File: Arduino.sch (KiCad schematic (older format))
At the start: 0 parts

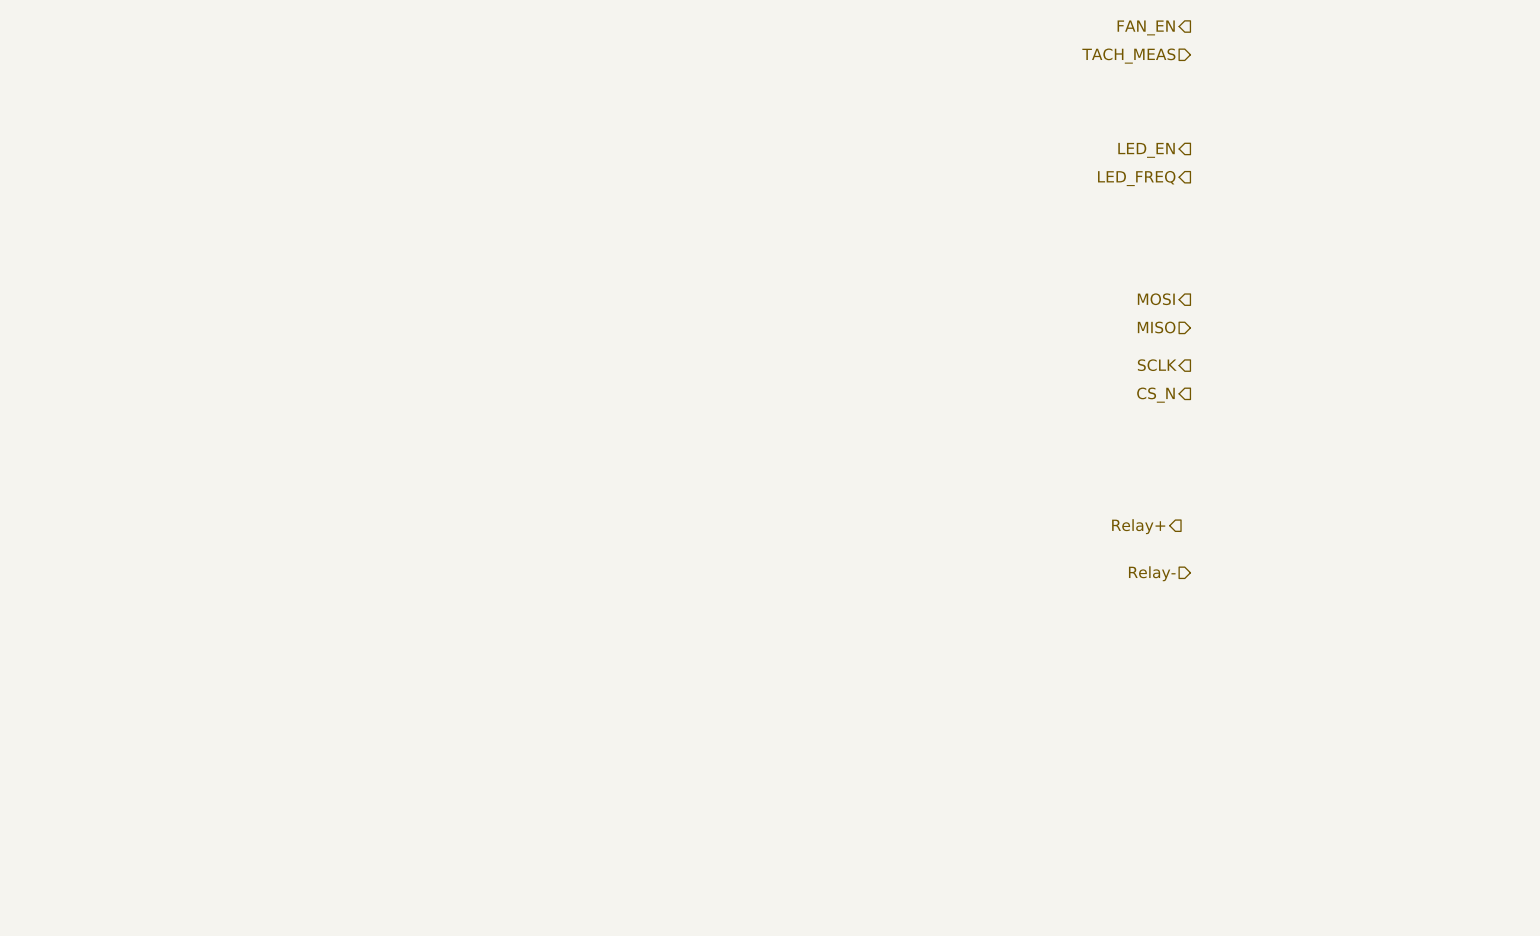
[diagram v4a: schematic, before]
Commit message: Create Arduino Schematic and Wire Up top Level
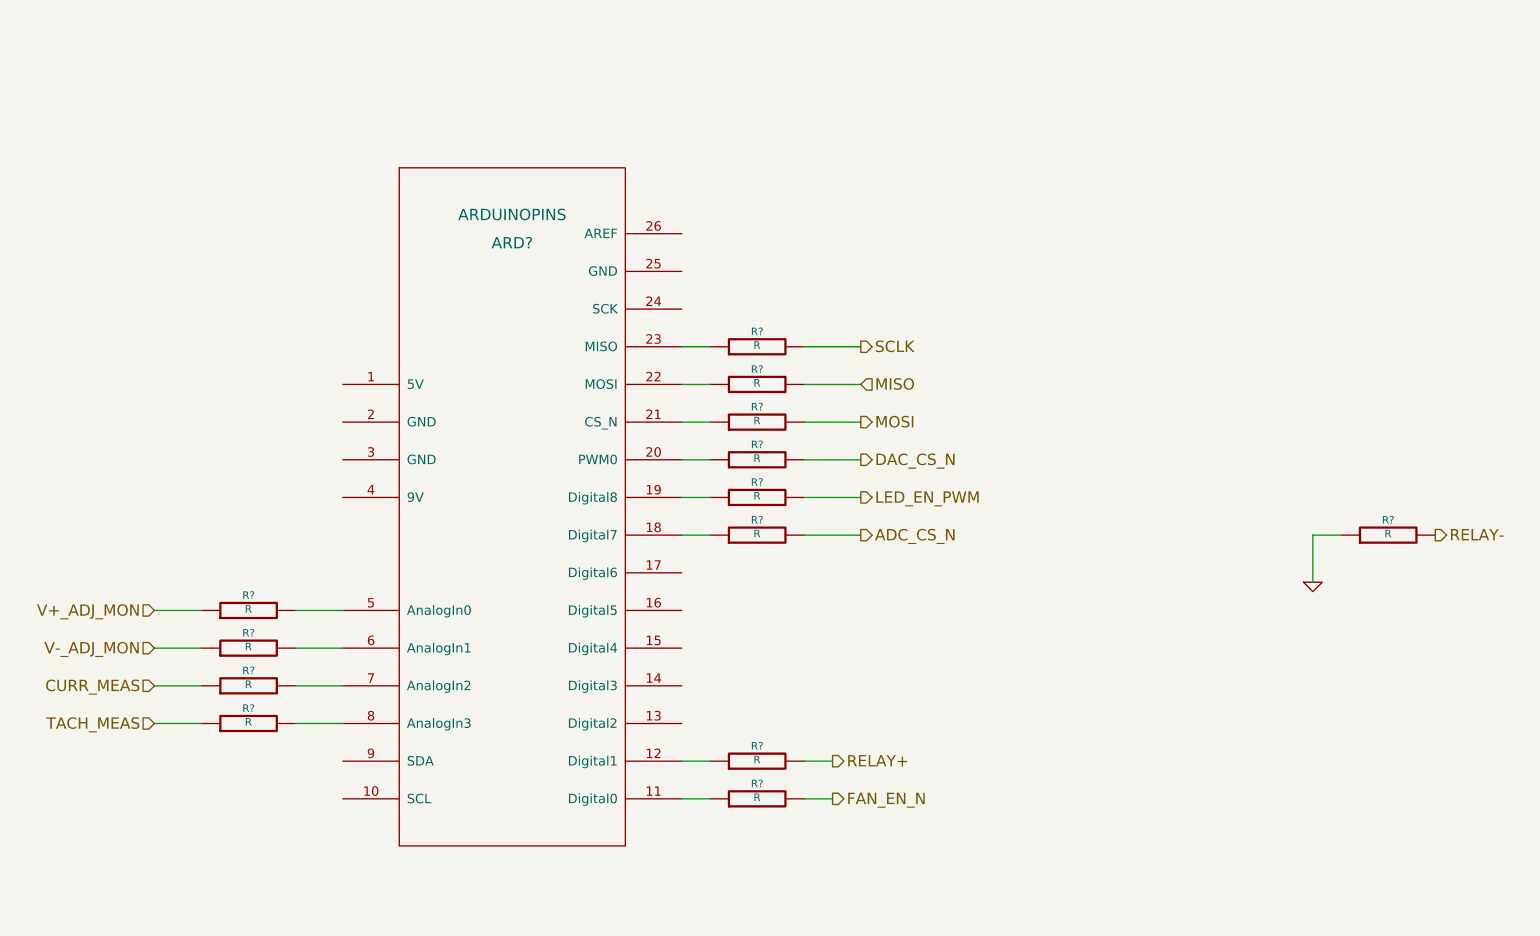
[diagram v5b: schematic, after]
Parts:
- added ARD?: ARDUINOPINS, symbol ARDUINOPINS
- added R? (x13): R, ~, symbol R
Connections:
- net MISO: now also R?.2
- net MOSI: now also R?.2
- net SCLK: now also R?.2
- net TACH_MEAS: now also R?.1
- new net: ARD?.11 (Digital0), R?.1
- new net: ARD?.12 (Digital1), R?.1
- new net: ARD?.18 (Digital7), R?.1
- new net: ARD?.19 (Digital8), R?.1
- new net: ARD?.20 (PWM0), R?.1
- new net: ARD?.21 (CS_N), R?.1
- new net: ARD?.22 (MOSI), R?.1
- new net: ARD?.23 (MISO), R?.1
- new net: ARD?.5 (AnalogIn0), R?.2
- new net: ARD?.6 (AnalogIn1), R?.2
- new net: ARD?.7 (AnalogIn2), R?.2
- new net: ARD?.8 (AnalogIn3), R?.2
- new net ADC_CS_N: R?.2
- new net CURR_MEAS: R?.1
- new net DAC_CS_N: R?.2
- new net FAN_EN_N: R?.2
- new net GND: R?.1
- new net LED_EN_PWM: R?.2
- new net RELAY+: R?.2
- new net RELAY-: R?.2
- new net V+_ADJ_MON: R?.1
- new net V-_ADJ_MON: R?.1

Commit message: Upgrade Current/Fan Output Schem Use PWM
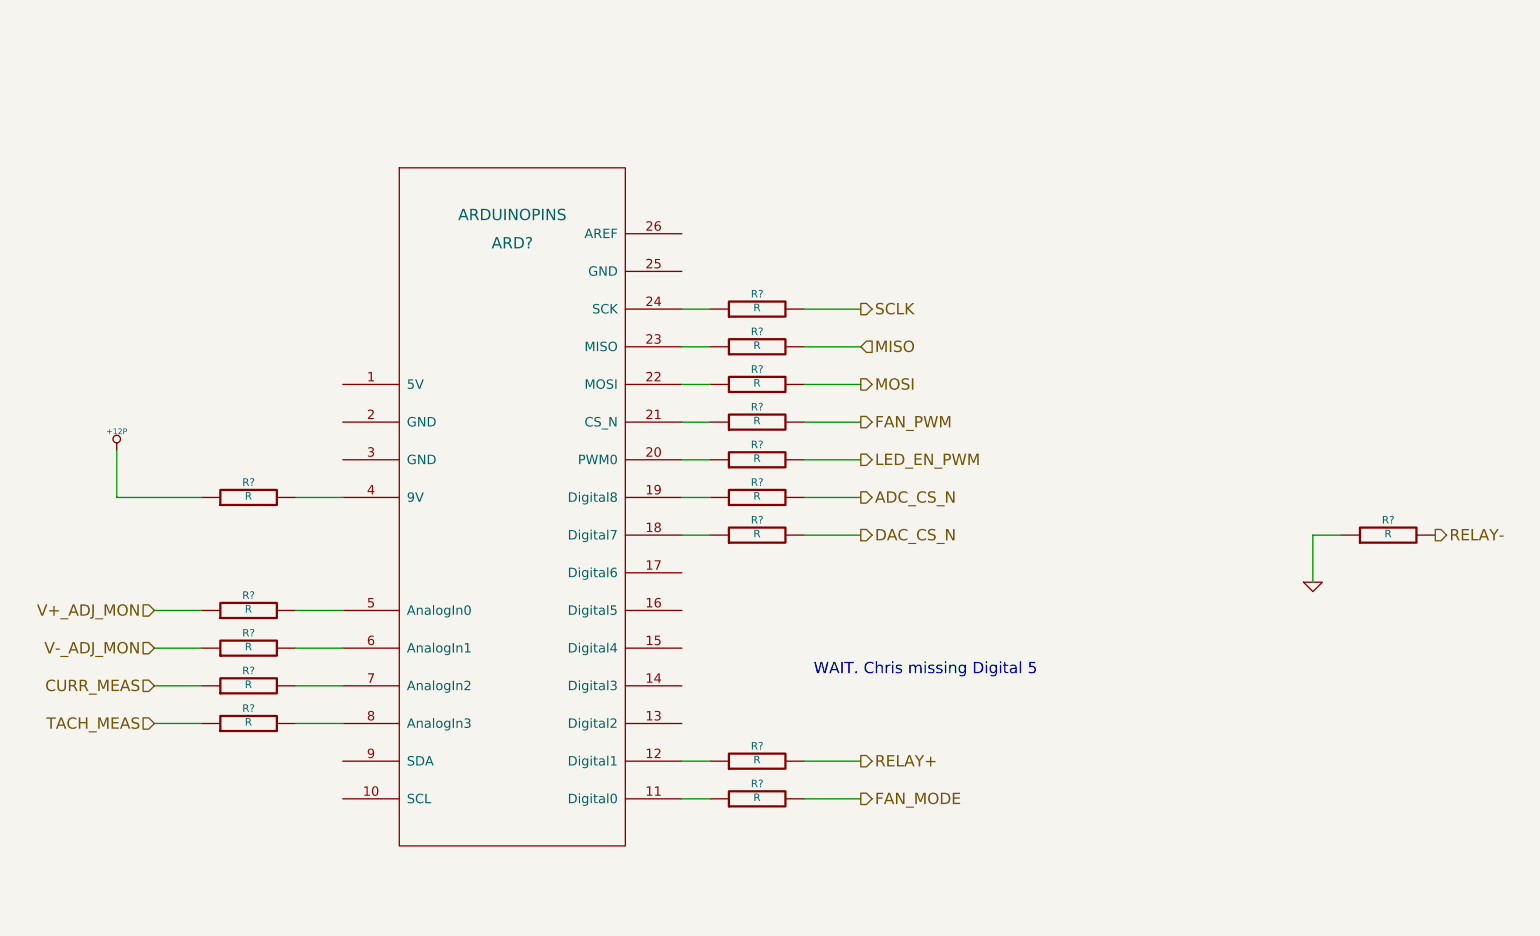
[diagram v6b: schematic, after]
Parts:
- removed ARD?: ARDUINOPINS, symbol ARDUINOPINS
- added ARD?: ARDUINOPINS, ~, symbol ARDUINOPINS
- added R? (x2): R, ~, symbol R
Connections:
- net at R?.1: now also ARD?.21 (CS_N)
- net at R?.1: now also ARD?.12 (Digital1)
- net at R?.1: now also ARD?.19 (Digital8)
- net at R?.1: now also ARD?.20 (PWM0)
- net at R?.1: now also ARD?.18 (Digital7)
- net at R?.1: now also ARD?.22 (MOSI)
- net at R?.1: now also ARD?.23 (MISO)
- net at R?.1: now also ARD?.24 (SCK)
- net at R?.2: now also ARD?.5 (AnalogIn0)
- net at R?.2: now also ARD?.6 (AnalogIn1)
- net at R?.2: now also ARD?.7 (AnalogIn2)
- net at R?.2: now also ARD?.8 (AnalogIn3)
- net FAN_EN_N renamed FAN_PWM
- new net: ARD?.11 (Digital0), R?.1
- new net: ARD?.4 (9V), R?.2
- new net +12P: R?.1
- new net FAN_MODE: R?.2
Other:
- note added: "WAIT. Chris missing Digital 5"
- moved on the sheet: R?
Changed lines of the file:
@@
 Sheet 2 9
 Title ""
-Date "5 feb 2014"
+Date "9 feb 2014"
 Rev ""
 Comp ""
@@
 Comment4 ""
 $EndDescr
-Text HLabel 6850 5650 2    60   Output ~ 0
+Text HLabel 7000 5650 2    60   Output ~ 0
 RELAY+
 Text HLabel 10050 4450 2    60   Output ~ 0
 RELAY-
+Text HLabel 7000 3650 2    60   Output ~ 0
+MOSI
+Text HLabel 7000 3450 2    60   Input ~ 0
+MISO
+Text HLabel 7000 3250 2    60   Output ~ 0
+SCLK
+Text HLabel 7000 4450 2    60   Output ~ 0
+DAC_CS_N
 Text HLabel 7000 3850 2    60   Output ~ 0
-MOSI
-Text HLabel 7000 3650 2    60   Input ~ 0
-MISO
-Text HLabel 7000 3450 2    60   Output ~ 0
-SCLK
-Text HLabel 7000 4050 2    60   Output ~ 0
-DAC_CS_N
-Text HLabel 6850 5850 2    60   Output ~ 0
-FAN_EN_N
+FAN_PWM
 Text HLabel 3250 5450 0    60   Input ~ 0
 TACH_MEAS
@@
 L R R?
 U 1 1 52F32414
-P 6450 5850
-F 0 "R?" V 6530 5850 40  0000 C CNN
-F 1 "R" V 6457 5851 40  0000 C CNN
-F 2 "~" V 6380 5850 30  0000 C CNN
-F 3 "~" H 6450 5850 30  0000 C CNN
-	1    6450 5850
+P 6450 3850
+F 0 "R?" V 6530 3850 40  0000 C CNN
+F 1 "R" V 6457 3851 40  0000 C CNN
+F 2 "~" V 6380 3850 30  0000 C CNN
+F 3 "~" H 6450 3850 30  0000 C CNN
+	1    6450 3850
 	0    -1   -1   0
 $EndComp
@@
 	9400 4450 9400 4700
 Wire Wire Line
+	6700 3250 7000 3250
+Wire Wire Line
 	6700 3450 7000 3450
 Wire Wire Line
 	6700 3650 7000 3650
 Wire Wire Line
+	6700 4450 7000 4450
+Wire Wire Line
+	7000 5650 6700 5650
+Wire Wire Line
 	6700 3850 7000 3850
 Wire Wire Line
-	6700 4050 7000 4050
-Wire Wire Line
-	6850 5650 6700 5650
-Wire Wire Line
-	6700 5850 6850 5850
-Wire Wire Line
 	6200 5650 6050 5650
 Wire Wire Line
-	6050 5850 6200 5850
-$Comp
-L ARDUINOPINS ARD?
-U 1 1 52F33825
-P 5200 4200
-F 0 "ARD?" H 5150 5500 60  0000 C CNN
-F 1 "ARDUINOPINS" H 5150 5650 60  0000 C CNN
-F 2 "" H 4900 4450 60  0000 C CNN
-F 3 "" H 4900 4450 60  0000 C CNN
-	1    5200 4200
-	1    0    0    -1
-$EndComp
+	6050 3850 6200 3850
 $Comp
 L R R?
@@
 L R R?
 U 1 1 52F34A10
-P 6450 4050
-F 0 "R?" V 6530 4050 40  0000 C CNN
-F 1 "R" V 6457 4051 40  0000 C CNN
-F 2 "~" V 6380 4050 30  0000 C CNN
-F 3 "~" H 6450 4050 30  0000 C CNN
-	1    6450 4050
+P 6450 4450
+F 0 "R?" V 6530 4450 40  0000 C CNN
+F 1 "R" V 6457 4451 40  0000 C CNN
+F 2 "~" V 6380 4450 30  0000 C CNN
+F 3 "~" H 6450 4450 30  0000 C CNN
+	1    6450 4450
 	0    -1   -1   0
 $EndComp
@@
 L R R?
 U 1 1 52F34A16
-P 6450 3850
-F 0 "R?" V 6530 3850 40  0000 C CNN
-F 1 "R" V 6457 3851 40  0000 C CNN
-F 2 "~" V 6380 3850 30  0000 C CNN
-F 3 "~" H 6450 3850 30  0000 C CNN
-	1    6450 3850
-	0    -1   -1   0
-$EndComp
-$Comp
-L R R?
-U 1 1 52F34A1C
 P 6450 3650
 F 0 "R?" V 6530 3650 40  0000 C CNN
@@
 $Comp
 L R R?
-U 1 1 52F34A22
+U 1 1 52F34A1C
 P 6450 3450
 F 0 "R?" V 6530 3450 40  0000 C CNN
@@
 	0    -1   -1   0
 $EndComp
-Wire Wire Line
-	6200 3450 6050 3450
-Wire Wire Line
-	6050 3650 6200 3650
-Wire Wire Line
-	6200 3850 6050 3850
-Wire Wire Line
-	6050 4050 6200 4050
+$Comp
+L R R?
+U 1 1 52F34A22
+P 6450 3250
+F 0 "R?" V 6530 3250 40  0000 C CNN
+F 1 "R" V 6457 3251 40  0000 C CNN
+F 2 "~" V 6380 3250 30  0000 C CNN
+F 3 "~" H 6450 3250 30  0000 C CNN
+	1    6450 3250
+	0    -1   -1   0
+$EndComp
+Wire Wire Line
+	6200 3250 6050 3250
+Wire Wire Line
+	6050 3450 6200 3450
+Wire Wire Line
+	6200 3650 6050 3650
+Wire Wire Line
+	6050 4450 6200 4450
 $Comp
 L R R?
@@
 L R R?
 U 1 1 52F34AE7
+P 6450 4050
+F 0 "R?" V 6530 4050 40  0000 C CNN
+F 1 "R" V 6457 4051 40  0000 C CNN
+F 2 "~" V 6380 4050 30  0000 C CNN
+F 3 "~" H 6450 4050 30  0000 C CNN
+	1    6450 4050
+	0    -1   -1   0
+$EndComp
+Wire Wire Line
+	6050 4050 6200 4050
+Text HLabel 7000 4050 2    60   Output ~ 0
+LED_EN_PWM
+Wire Wire Line
+	6700 4050 7000 4050
+Text HLabel 7000 4250 2    60   Output ~ 0
+ADC_CS_N
+$Comp
+L R R?
+U 1 1 52F37027
 P 6450 4250
 F 0 "R?" V 6530 4250 40  0000 C CNN
@@
 $EndComp
 Wire Wire Line
-	6050 4250 6200 4250
-Text HLabel 7000 4250 2    60   Output ~ 0
-LED_EN_PWM
-Wire Wire Line
-	6700 4250 7000 4250
-Text HLabel 7000 4450 2    60   Output ~ 0
-ADC_CS_N
-$Comp
-L R R?
-U 1 1 52F37027
-P 6450 4450
-F 0 "R?" V 6530 4450 40  0000 C CNN
-F 1 "R" V 6457 4451 40  0000 C CNN
-F 2 "~" V 6380 4450 30  0000 C CNN
-F 3 "~" H 6450 4450 30  0000 C CNN
-	1    6450 4450
-	0    -1   -1   0
-$EndComp
-Wire Wire Line
-	6200 4450 6050 4450
-Wire Wire Line
-	7000 4450 6700 4450
+	6200 4250 6050 4250
+Wire Wire Line
+	7000 4250 6700 4250
+Text HLabel 7000 5850 2    60   Output ~ 0
+FAN_MODE
+Wire Wire Line
+	6700 5850 7000 5850
+$Comp
+L R R?
+U 1 1 52F7B7CD
+P 6450 5850
+F 0 "R?" V 6530 5850 40  0000 C CNN
+F 1 "R" V 6457 5851 40  0000 C CNN
+F 2 "~" V 6380 5850 30  0000 C CNN
+F 3 "~" H 6450 5850 30  0000 C CNN
+	1    6450 5850
+	0    -1   -1   0
+$EndComp
+Wire Wire Line
+	6050 5850 6200 5850
+Text Notes 6750 5200 0    60   ~ 0
+WAIT. Chris missing Digital 5
+$Comp
+L R R?
+U 1 1 52F7B7D5
+P 3750 4250
+F 0 "R?" V 3830 4250 40  0000 C CNN
+F 1 "R" V 3757 4251 40  0000 C CNN
+F 2 "~" V 3680 4250 30  0000 C CNN
+F 3 "~" H 3750 4250 30  0000 C CNN
+	1    3750 4250
+	0    -1   -1   0
+$EndComp
+Wire Wire Line
+	4250 4250 4000 4250
+$Comp
+L +12P #PWR?
+U 1 1 52F7B7FA
+P 3050 4000
+F 0 "#PWR?" H 3050 3970 30  0001 C CNN
+F 1 "+12P" H 3050 4100 30  0000 C CNN
+F 2 "" H 3050 4000 60  0000 C CNN
+F 3 "" H 3050 4000 60  0000 C CNN
+	1    3050 4000
+	1    0    0    -1
+$EndComp
+Wire Wire Line
+	3050 4000 3050 4250
+Wire Wire Line
+	3050 4250 3500 4250
+$Comp
+L ARDUINOPINS ARD?
+U 1 1 52F7C9A3
+P 5200 4200
+F 0 "ARD?" H 5150 5500 60  0000 C CNN
+F 1 "ARDUINOPINS" H 5150 5650 60  0000 C CNN
+F 2 "~" H 4900 4450 60  0000 C CNN
+F 3 "~" H 4900 4450 60  0000 C CNN
+	1    5200 4200
+	1    0    0    -1
+$EndComp
 $EndSCHEMATC
